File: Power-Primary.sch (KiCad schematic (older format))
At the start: 45 parts, among them J1 HV in, J10 SPARE, J11 SPARE, J2 Dashboard, J3 Telemetry, J4 Motor, J5 MPPT 1, J6 MPPT 2, J7 BPS, J8 Primary Disconn., J9 SPARE, U1 Mean_Well_12V

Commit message: Renames project name to Power-Primary and fixes library issues
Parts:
- U1: footprint Power Board Parts:DC-DC Converter 12V -> UTSVT_Power:Mean_Well_12V; symbol New-Power-Distribution-Board-rescue:Mean_Well_12V-vicor_mini_12v -> utsvt-power-regulators:Mean_Well_12V-vicor_mini_12v
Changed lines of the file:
@@
 	4000 4150 4000 4500
 $Comp
-L New-Power-Distribution-Board-rescue:Mean_Well_12V-vicor_mini_12v U1
+L utsvt-power-regulators:Mean_Well_12V-vicor_mini_12v U1
 U 1 1 5BE09B68
 P 2100 4800
 F 0 "U1" H 2950 6587 60  0000 C CNN
 F 1 "Mean_Well_12V" H 2950 6481 60  0000 C CNN
-F 2 "Power Board Parts:DC-DC Converter 12V" H 2100 4800 60  0001 C CNN
+F 2 "UTSVT_Power:Mean_Well_12V" H 2100 4800 60  0001 C CNN
 F 3 "" H 2100 4800 60  0001 C CNN
 	1    2100 4800

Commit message: Practice push + changed schematic
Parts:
- added D11, D12, D13, D14, D15, D16: LED, LED_THT:LED_D3.0mm, symbol Device:LED
- added F12: MPPT 2, Fuse:Fuseholder_Blade_Mini_Keystone_3568, symbol Device:Fuse
- added F13: BPS, Fuse:Fuseholder_Blade_Mini_Keystone_3568, symbol Device:Fuse
- added F14: Primary Disconn., Fuse:Fuseholder_Blade_Mini_Keystone_3568, symbol Device:Fuse
- added F15, F16, F17: SPARE, Fuse:Fuseholder_Blade_Mini_Keystone_3568, symbol Device:Fuse
- added J12, J13, J14, J15, J? (x2): SPARE, Connector_Molex:Molex_Micro-Fit_3.0_43650-0215_1x02_P3.00mm_Vertical, symbol Connector:Conn_01x02_Female
- added R11, R12, R13 (x2), R14 (x2): 11K, Resistor_THT:R_Axial_DIN0204_L3.6mm_D1.6mm_P7.62mm_Horizontal, symbol Device:R
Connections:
- wire segments 120 -> 190
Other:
- moved on the sheet: D1, D10, D11, D2, D3, D4, D5, D6, D7, D8, D9, F1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

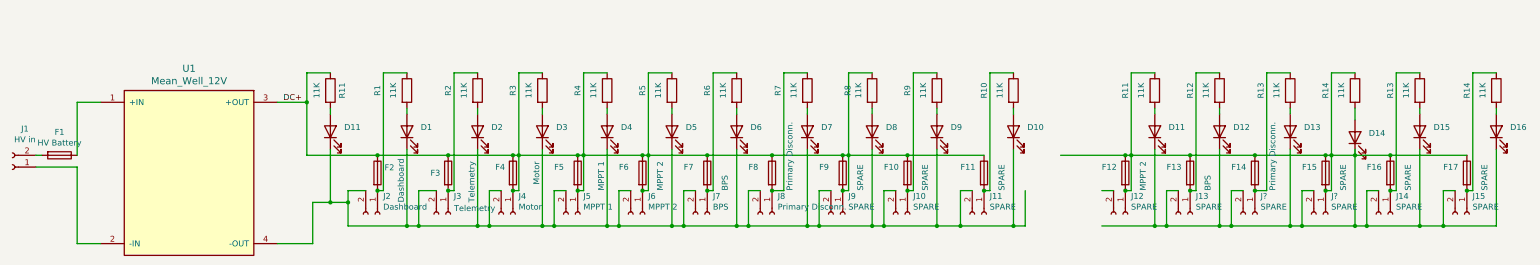
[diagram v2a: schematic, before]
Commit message: schematic almost done, connection errors
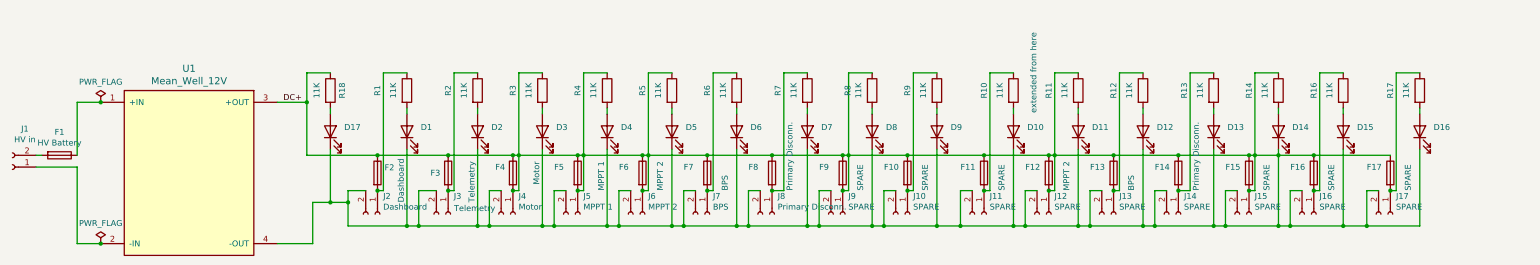
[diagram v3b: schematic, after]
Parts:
- gave numbers to parts that had none: 2
- renumbered D11 to D17, J14 to J16, J15 to J17, R13 to R16, R14 to R17, R11 to R18
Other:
- note added: "extended from here"
- moved on the sheet: D11, D12, D13, D14, D15, D16, F12, F13, F14, F15, F16, F17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

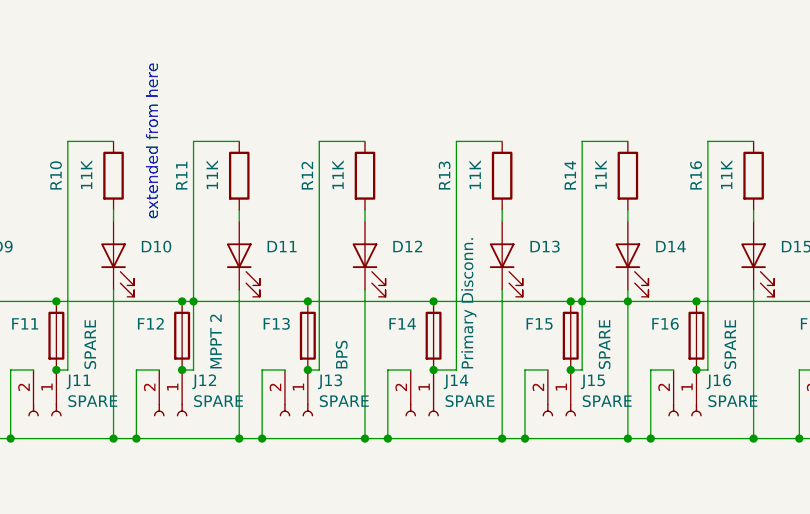
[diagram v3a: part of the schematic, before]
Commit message: schematic done, U1 pin 3/4 error
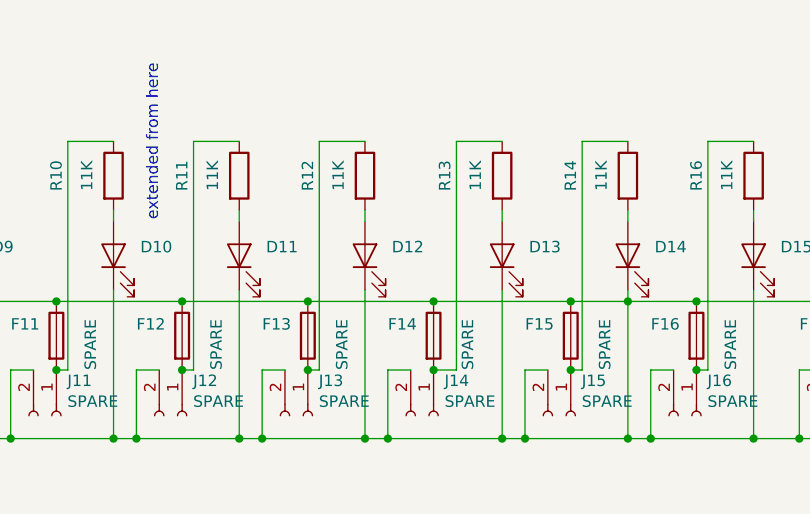
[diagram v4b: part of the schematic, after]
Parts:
- F12: value MPPT 2 -> SPARE
- F13: value BPS -> SPARE
- F14: value Primary Disconn. -> SPARE
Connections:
- net DC+: no longer F12.2, F15.2, J12.1 (Pin_1), J15.1 (Pin_1), R11.1, R14.1
- new net: F12.2, J12.1 (Pin_1), R11.1
- new net: F15.2, J15.1 (Pin_1), R14.1

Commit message: finished schematic
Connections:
- net DC+: no longer D1.1 (K), D10.1 (K), D11.1 (K), D12.1 (K), D13.1 (K), D14.1 (K), D15.1 (K), D16.1 (K), D17.1 (K), D2.1 (K), D3.1 (K), D4.1 (K), D5.1 (K), D6.1 (K), D7.1 (K), D8.1 (K), D9.1 (K), F4.2, F5.2, F6.2, F9.2, J10.2 (Pin_2), J11.2 (Pin_2), J12.2 (Pin_2), J13.2 (Pin_2), J14.2 (Pin_2), J15.2 (Pin_2), J16.2 (Pin_2), J17.2 (Pin_2), J2.2 (Pin_2), J3.2 (Pin_2), J4.1 (Pin_1), J4.2 (Pin_2), J5.1 (Pin_1), J5.2 (Pin_2), J6.1 (Pin_1), J6.2 (Pin_2), J7.2 (Pin_2), J8.2 (Pin_2), J9.1 (Pin_1), J9.2 (Pin_2), R3.1, R4.1, R5.1, R8.1, U1.4 (-OUT)
- new net: F4.2, J4.1 (Pin_1), R3.1
- new net: F5.2, J5.1 (Pin_1), R4.1
- new net: F6.2, J6.1 (Pin_1), R5.1
- new net: D1.1 (K), D10.1 (K), D11.1 (K), D12.1 (K), D13.1 (K), D14.1 (K), D15.1 (K), D16.1 (K), D17.1 (K), D2.1 (K), D3.1 (K), D4.1 (K), D5.1 (K), D6.1 (K), D7.1 (K), D8.1 (K), D9.1 (K), J10.2 (Pin_2), J11.2 (Pin_2), J12.2 (Pin_2), J13.2 (Pin_2), J14.2 (Pin_2), J15.2 (Pin_2), J16.2 (Pin_2), J17.2 (Pin_2), J2.2 (Pin_2), J3.2 (Pin_2), J4.2 (Pin_2), J5.2 (Pin_2), J6.2 (Pin_2), J7.2 (Pin_2), J8.2 (Pin_2), J9.2 (Pin_2), U1.4 (-OUT)
- new net: F9.2, J9.1 (Pin_1), R8.1

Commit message: finished PCB waiting for edits
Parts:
- renumbered R16 to R15, R17 to R16
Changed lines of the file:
@@
 	13300 3700 13500 3700
 $Comp
-L Device:R R17
+L Device:R R16
 U 1 1 5F66DBBF
 P 13500 3850
-F 0 "R17" V 13250 3850 50  0000 C CNN
+F 0 "R16" V 13250 3850 50  0000 C CNN
 F 1 "11K" V 13384 3850 50  0000 C CNN
 F 2 "Resistor_THT:R_Axial_DIN0204_L3.6mm_D1.6mm_P7.62mm_Horizontal" V 13430 3850 50  0001 C CNN
@@
 $EndComp
 $Comp
-L Device:R R16
+L Device:R R15
 U 1 1 5F66DBA1
 P 12850 3850
-F 0 "R16" V 12600 3850 50  0000 C CNN
+F 0 "R15" V 12600 3850 50  0000 C CNN
 F 1 "11K" V 12734 3850 50  0000 C CNN
 F 2 "Resistor_THT:R_Axial_DIN0204_L3.6mm_D1.6mm_P7.62mm_Horizontal" V 12780 3850 50  0001 C CNN

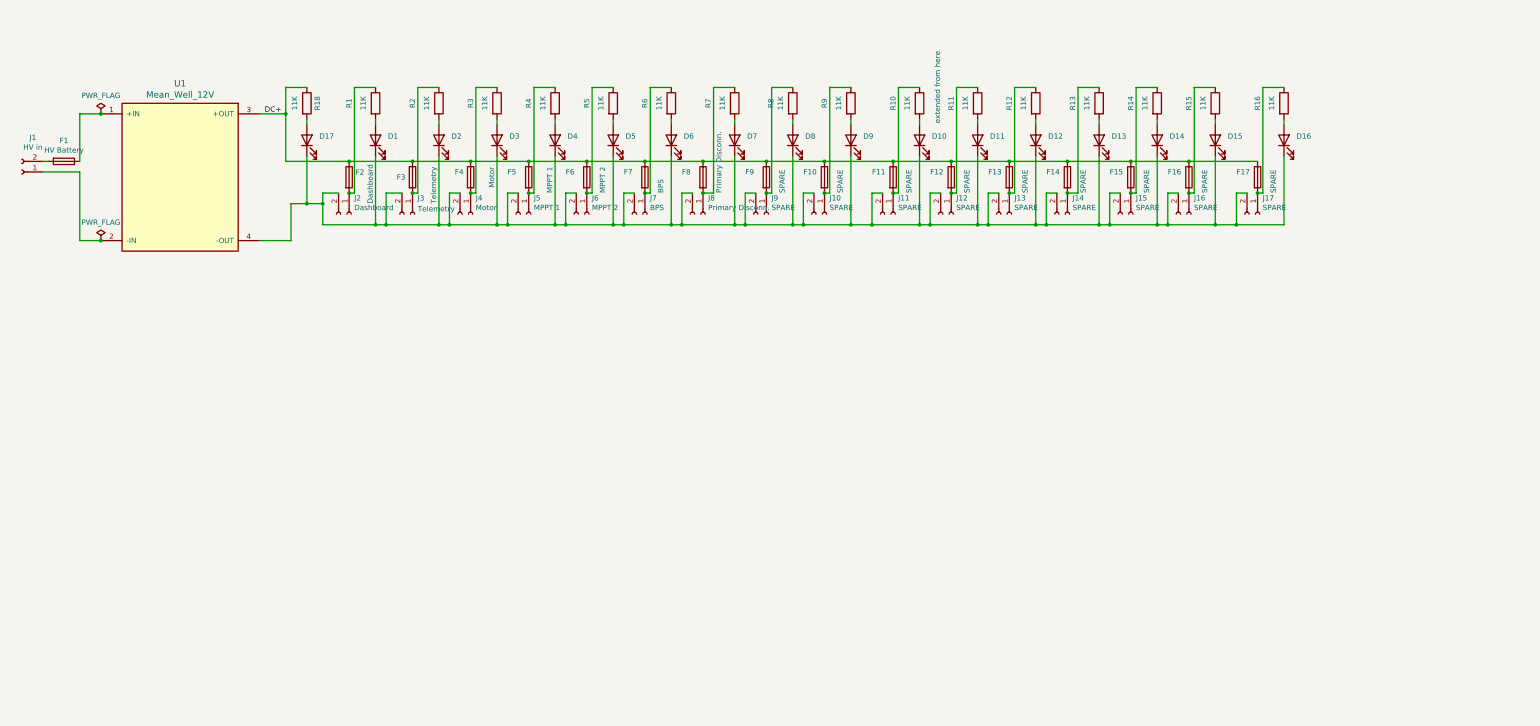
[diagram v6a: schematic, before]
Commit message: Adds pdf and png documentation files of schematic and pcb
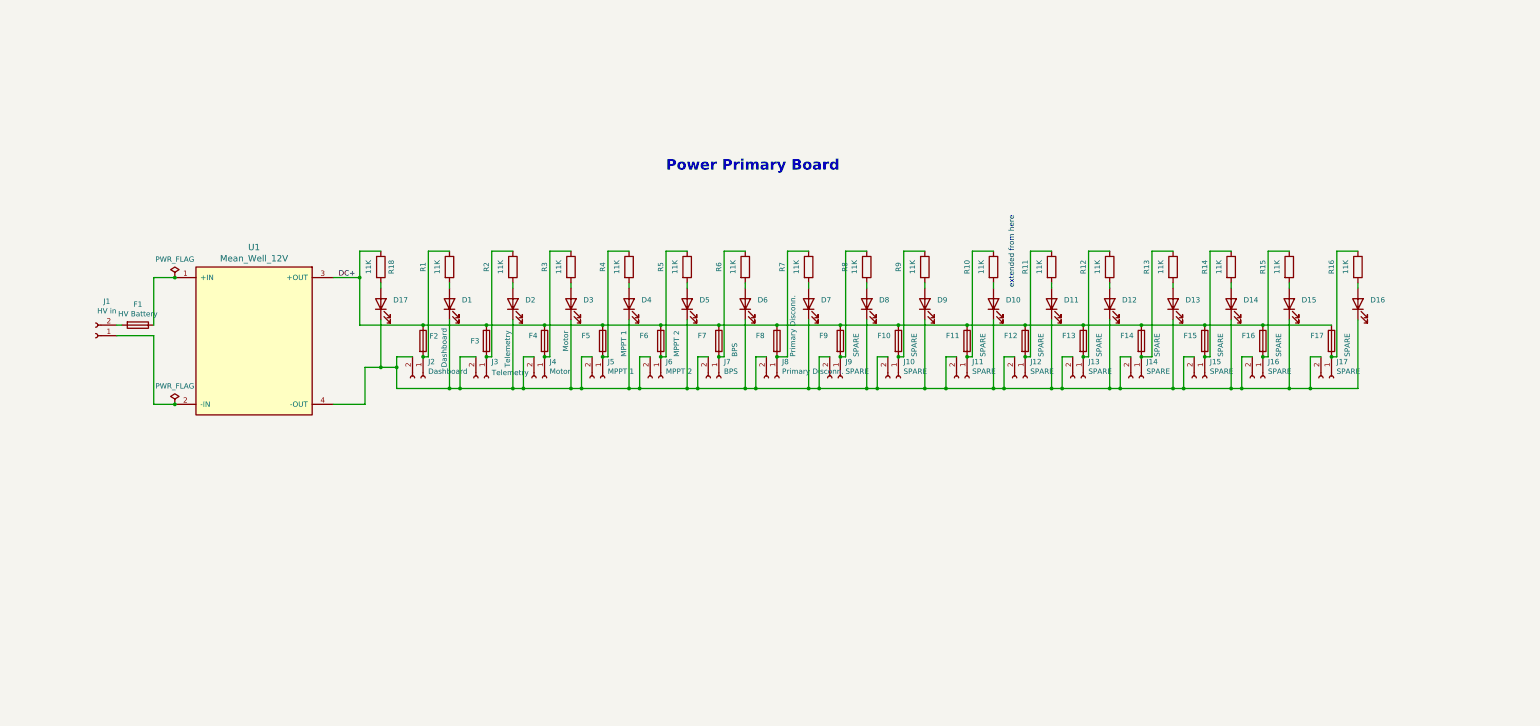
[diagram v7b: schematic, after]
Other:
- note added: "Power Primary Board"
- moved on the sheet: D1, D10, D11, D12, D13, D14, D15, D16, D17, D2, D3, D4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

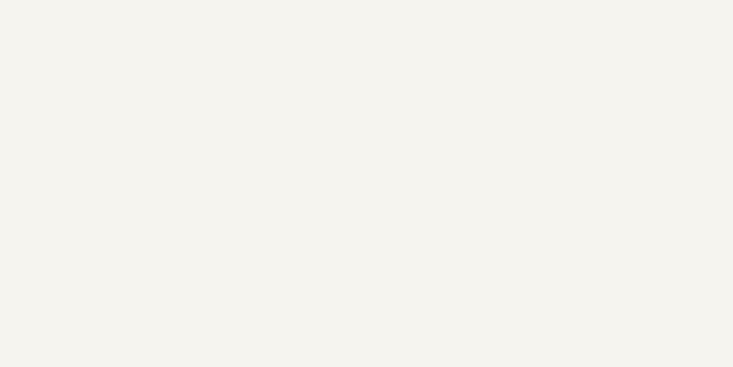
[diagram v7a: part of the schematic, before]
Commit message: Added mounting holes and updated pcb/sch
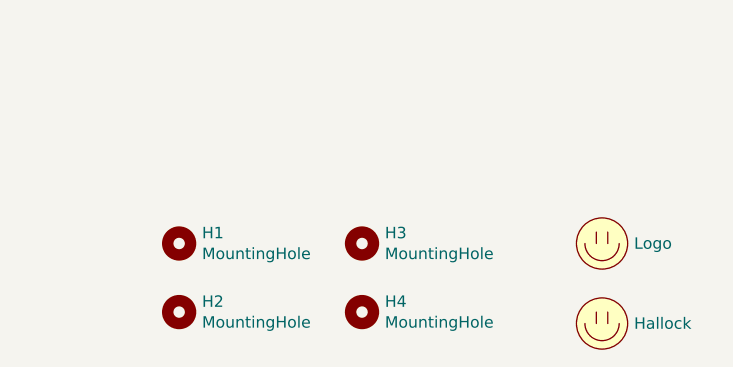
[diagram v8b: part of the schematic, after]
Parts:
- added H1, H2, H3, H4: MountingHole, MountingHole:MountingHole_3mm, symbol Mechanical:MountingHole
- added LOGO1: Logo, UTSVT_Special:UTSVT_Logo_Symbol, symbol utsvt-misc:Logo_Placeholder
- added LOGO2: Hallock, UTSVT_Special:Hallock_Image, symbol utsvt-misc:Logo_Placeholder
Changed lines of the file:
@@
 Text Notes 7650 4500 0    100  ~ 20
 Power Primary Board
+$Comp
+L Mechanical:MountingHole H1
+U 1 1 5FC30C37
+P 13500 9200
+F 0 "H1" H 13600 9246 50  0000 L CNN
+F 1 "MountingHole" H 13600 9155 50  0000 L CNN
+F 2 "MountingHole:MountingHole_3mm" H 13500 9200 50  0001 C CNN
+F 3 "~" H 13500 9200 50  0001 C CNN
+	1    13500 9200
+	1    0    0    -1
+$EndComp
+$Comp
+L Mechanical:MountingHole H2
+U 1 1 5FC31367
+P 13500 9500
+F 0 "H2" H 13600 9546 50  0000 L CNN
+F 1 "MountingHole" H 13600 9455 50  0000 L CNN
+F 2 "MountingHole:MountingHole_3mm" H 13500 9500 50  0001 C CNN
+F 3 "~" H 13500 9500 50  0001 C CNN
+	1    13500 9500
+	1    0    0    -1
+$EndComp
+$Comp
+L Mechanical:MountingHole H3
+U 1 1 5FC386D8
+P 14300 9200
+F 0 "H3" H 14400 9246 50  0000 L CNN
+F 1 "MountingHole" H 14400 9155 50  0000 L CNN
+F 2 "MountingHole:MountingHole_3mm" H 14300 9200 50  0001 C CNN
+F 3 "~" H 14300 9200 50  0001 C CNN
+	1    14300 9200
+	1    0    0    -1
+$EndComp
+$Comp
+L Mechanical:MountingHole H4
+U 1 1 5FC386DE
+P 14300 9500
+F 0 "H4" H 14400 9546 50  0000 L CNN
+F 1 "MountingHole" H 14400 9455 50  0000 L CNN
+F 2 "MountingHole:MountingHole_3mm" H 14300 9500 50  0001 C CNN
+F 3 "~" H 14300 9500 50  0001 C CNN
+	1    14300 9500
+	1    0    0    -1
+$EndComp
+$Comp
+L utsvt-misc:Logo_Placeholder LOGO1
+U 1 1 5FC48B47
+P 15350 9200
+F 0 "LOGO1" H 15350 9350 50  0001 C CNN
+F 1 "Logo" H 15490 9200 50  0000 L CNN
+F 2 "UTSVT_Special:UTSVT_Logo_Symbol" H 15350 9275 50  0001 C CNN
+F 3 "" H 15350 9275 50  0001 C CNN
+	1    15350 9200
+	1    0    0    -1
+$EndComp
+$Comp
+L utsvt-misc:Logo_Placeholder LOGO2
+U 1 1 5FC497EC
+P 15350 9550
+F 0 "LOGO2" H 15350 9700 50  0001 C CNN
+F 1 "Hallock" H 15490 9550 50  0000 L CNN
+F 2 "UTSVT_Special:Hallock_Image" H 15350 9625 50  0001 C CNN
+F 3 "" H 15350 9625 50  0001 C CNN
+	1    15350 9550
+	1    0    0    -1
+$EndComp
 $EndSCHEMATC
